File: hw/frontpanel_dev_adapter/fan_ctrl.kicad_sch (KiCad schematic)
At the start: 11 parts, among them M401 Fan_4pin, Q401 AO3400A, U401 74LVC2G17gw

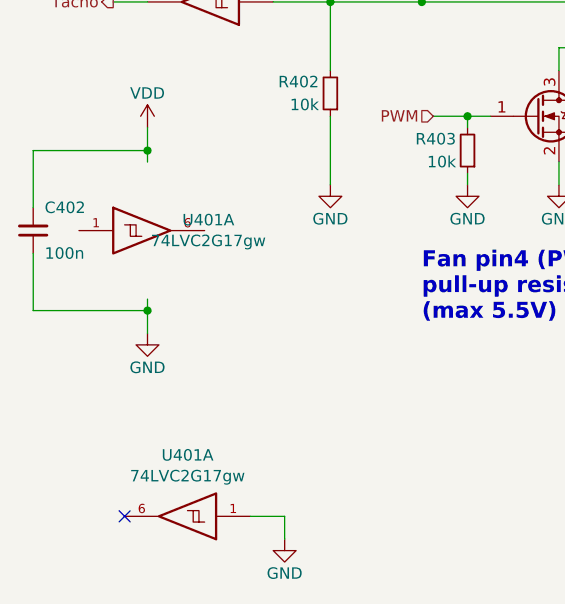
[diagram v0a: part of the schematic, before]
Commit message: hw: long-standing uncommitted stuff; mostly auto-updates (v7) fw: remove L052 tree (CMSIS & std-HAL shouldn't be committed and it was the wrong device name anyway)
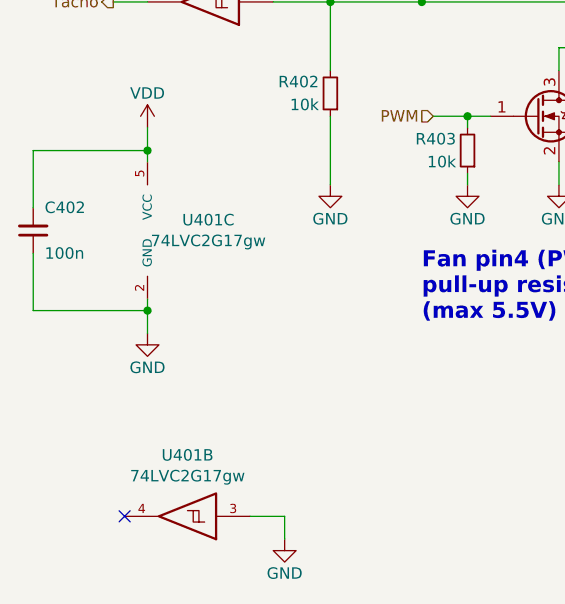
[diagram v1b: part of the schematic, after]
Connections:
- net GND: now also U401.2 (GND), U401.3; no longer U401.1
- net VDD: now also U401.5 (VCC)
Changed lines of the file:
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@@
     (pin "1")
   )
-  (symbol (lib_id "customlib_mj:74LVC2G17") (at 76.2 130.81 0) (unit 1)
+  (symbol (lib_id "customlib_mj:74LVC2G17") (at 76.2 130.81 0) (unit 3)
     (in_bom yes) (on_board yes)
     (property "Reference" "U401" (id 0) (at 82.9564 129.6416 0))
@@
       (effects (font (size 1.27 1.27)) hide)
     )
-    (pin "1")
-    (pin "6")
+    (pin "2")
+    (pin "5")
   )
   (symbol (lib_id "power:VDD") (at 76.2 119.38 0) (unit 1)
@@
     (pin "2")
   )
-  (symbol (lib_id "customlib_mj:74LVC2G17") (at 80.01 162.56 180) (unit 1)
+  (symbol (lib_id "customlib_mj:74LVC2G17") (at 80.01 162.56 180) (unit 2)
     (in_bom yes) (on_board yes)
     (property "Reference" "U401" (id 0) (at 80.645 155.7782 0))
@@
       (effects (font (size 1.27 1.27)) hide)
     )
-    (pin "1")
-    (pin "6")
+    (pin "3")
+    (pin "4")
   )
   (symbol (lib_id "power:GND") (at 91.44 165.1 0) (unit 1)

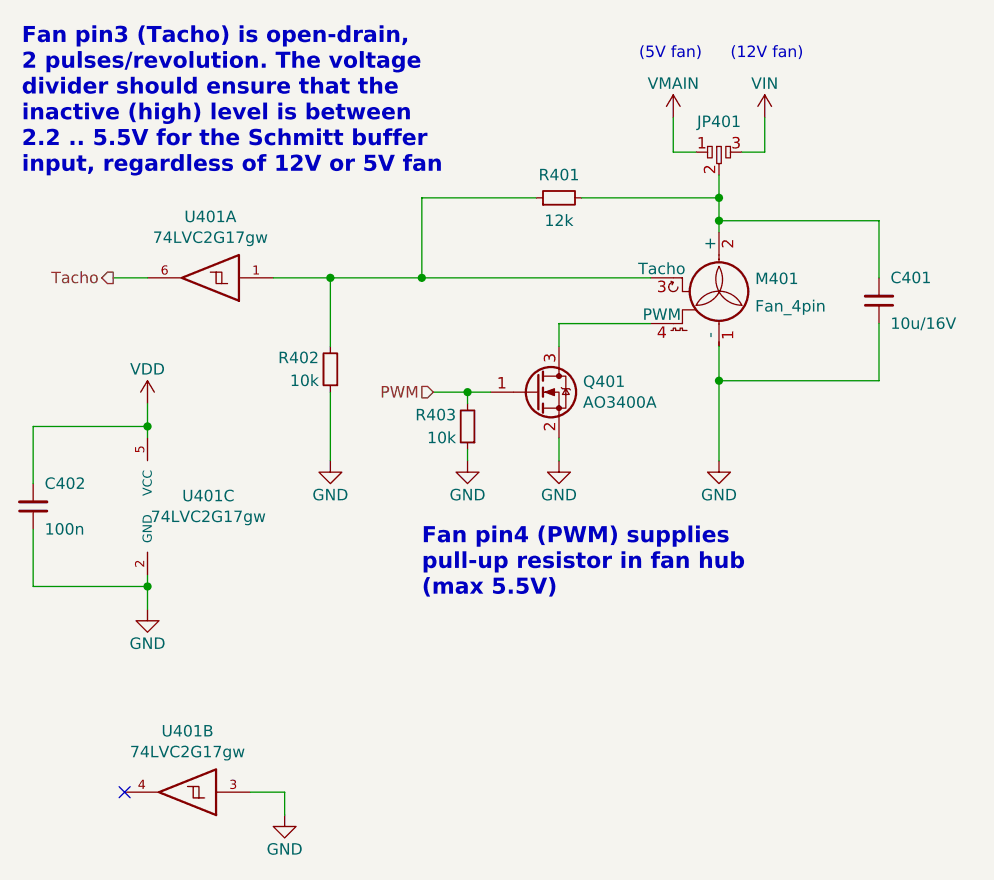
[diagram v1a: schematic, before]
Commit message: Various boards & schematics (auto-)updated to Kicad-v8
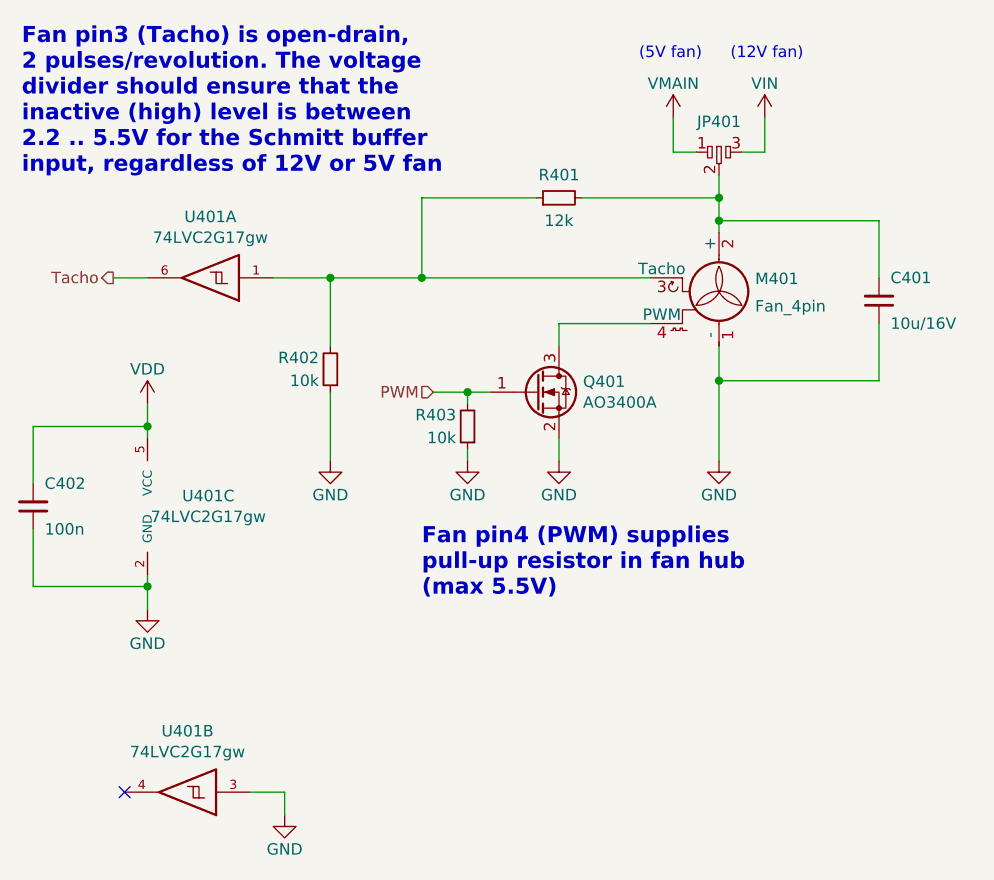
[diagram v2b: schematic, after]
